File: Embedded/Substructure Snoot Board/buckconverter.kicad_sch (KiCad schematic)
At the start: 33 parts, among them U10 LM5176PWP

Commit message: Added Buck Converter Component Values
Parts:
- removed D3: D_Schottky, symbol Device:D_Schottky
- added C24, C25: 33uF 40mohm, symbol Device:C_Polarized
- added C26: 6.8nF 523mohm, symbol Device:C
- added D3: 500mV 200mA, symbol Device:D
- added Q1, Q2, Q4: CSD17577Q5A, Package_TO_SOT_SMD:TDSON-8-1, symbol Transistor_FET:CSD17577Q5A
- added Q3: CSD17573Q5B, Package_TO_SOT_SMD:TDSON-8-1, symbol Transistor_FET:CSD17573Q5B
- added R18: 4.8m, symbol Device:R
- C10: value C -> 2nF 0ohm
- C11: value C -> 82pF 0ohm
- C12: value C -> 47pF 1mohms
- C13: value C_Polarized -> 33uF 40mohm
- C14, C19: value C -> 47uF 3mohm
- C15: value C -> 100nF 39mohm
- C16, C17, C18: value C -> 22uF 3.71mohm
- C20: value C -> 1uF 11.4mohm
- C21, C22: value C -> 100nF 50mohm
- C23: value C -> 100nF 1mohm
- C8: value C -> 15nF 0ohm
- C9: value C -> 6.8nF 523mohm
- D1, D2: value D_Schottky -> 385mV 500mA
- L1: value L -> 1uH 2.6mohm
- R10, R9: value R -> 100
- R11: value R -> 249K
- R12: value R -> 110K
- R13: value R -> 2K
- R14: value R -> 10
- R15, R16: value R -> 105K
- R17: value R -> 10K
- R6: value R -> 732
- R7: value R -> 93.1K
- R8: value R -> 13K
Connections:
- net GND: now also C19.2, R10.2, R16.2, C24.2, C25.2, R18.2
- net Power Input: now also C24.1, C25.1, Q1.5 (D)
- net Power Output: now also Q3.5 (D)
- net at C20.1, D2.2 (A), R17.1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: now also D3.2 (A)
- net at C21.1, U10.20 (BOOT2): now also D3.1 (K)
- net at C21.2, U10.18 (SW2): now also L1.2, Q3.1 (S), Q3.2 (S), Q3.3 (S), Q4.5 (D)
- net at R9.2: now also Q2.1 (S), Q2.2 (S), Q2.3 (S), Q4.1 (S), Q4.2 (S), Q4.3 (S), R18.1
- net at C9.2, R6.1: now also C26.2
- net at C22.2, U10.28 (SW1): now also L1.1, Q1.1 (S), Q1.2 (S), Q1.3 (S), Q2.5 (D)
- net at C10.1, C9.1, U10.9 (COMP): now also C26.1
- net at U10.19 (HDRV2): now also Q3.4 (G)
- net at U10.21 (LDRV2): now also Q4.4 (G)
- net at U10.25 (LDRV1): now also Q2.4 (G)
- net at U10.27 (HDRV1): now also Q1.4 (G)
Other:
- moved on the sheet: C10, C11, C12, C13, C14, C15, C16, C17, C18, C19, C20, C21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

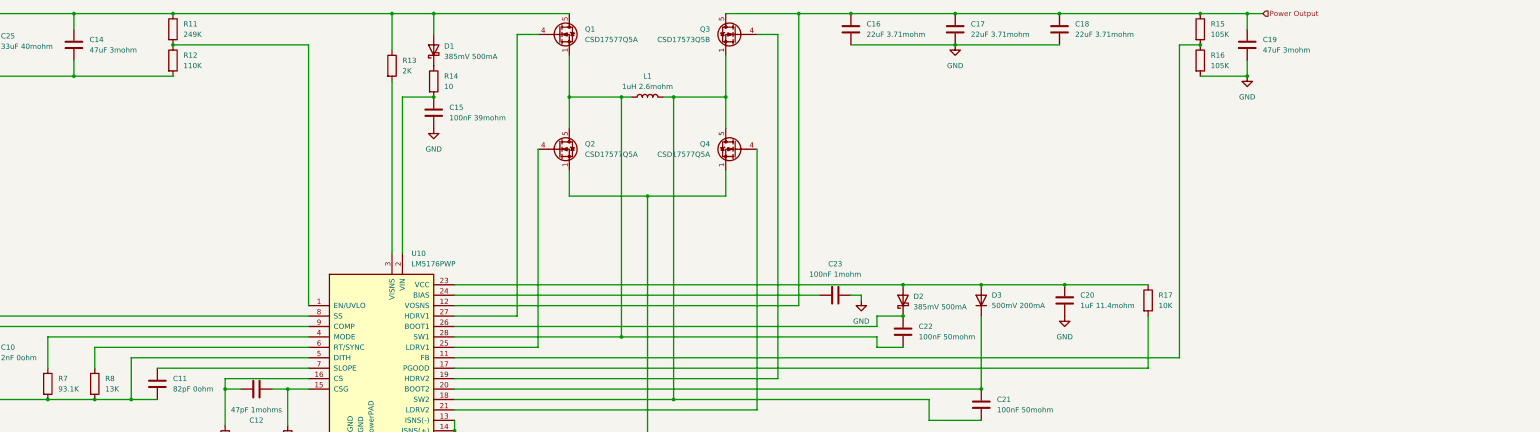
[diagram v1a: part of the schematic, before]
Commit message: Modified Buck Converter (Added Duplicate Components from Reference Design)
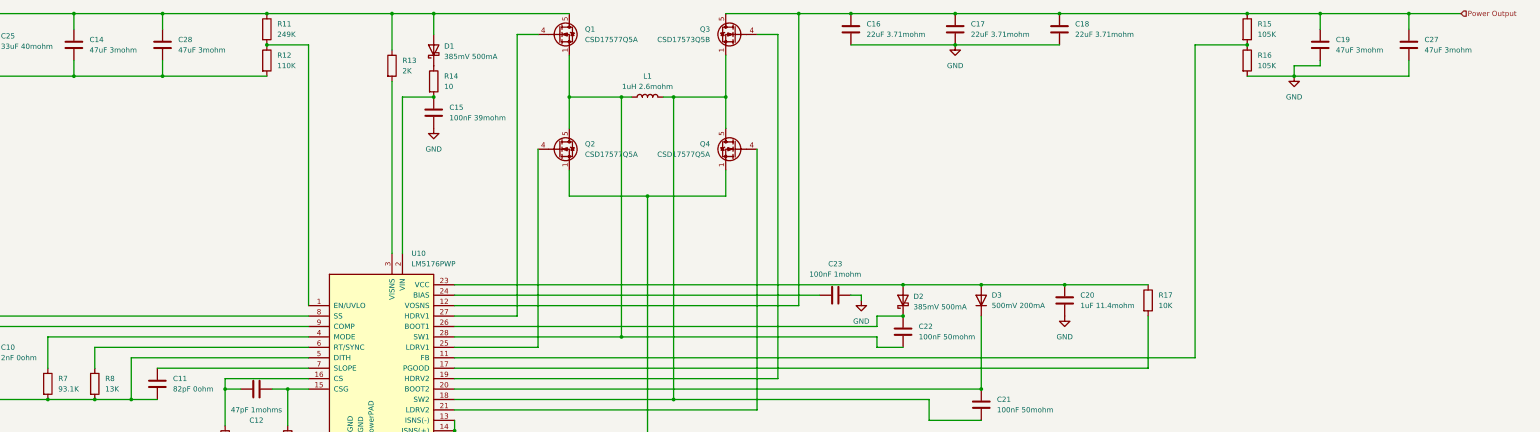
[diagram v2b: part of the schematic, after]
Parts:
- added C27, C28: 47uF 3mohm, symbol Device:C
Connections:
- net GND: now also C27.2, C28.2
- net Power Input: now also C28.1
- net Power Output: now also C27.1
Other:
- moved on the sheet: C19, R11, R12, R15, R16

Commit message: Added Footprints to the Input Power Filtering (Buck Converter)
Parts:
- C13, C24, C25: footprint (none) -> Capacitors:EEFCX1E330R
- C14, C28: footprint (none) -> Capacitor_SMD:C_1210_3225Metric_Pad1.33x2.70mm_HandSolder
- R11, R12: footprint (none) -> Capacitor_SMD:C_0402_1005Metric_Pad0.74x0.62mm_HandSolder
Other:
- moved on the sheet: C10, C11, C12, C13, C14, C15, C16, C17, C18, C19, C20, C21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

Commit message: Added LCSC Parts to Power Input, VCC and Mosfets (Buck Converter)
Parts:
- C13, C24, C25: LCSC (none) -> C193237
- C14, C28: LCSC (none) -> C77101
- C15: footprint (none) -> Resistor_SMD:R_0402_1005Metric_Pad0.72x0.64mm_HandSolder; LCSC (none) -> C2181865
- D1: LCSC (none) -> C155367
- L1: footprint (none) -> Inductors:XAL7070-102ME; LCSC (none) -> C6609502
- Q1, Q2, Q4: LCSC (none) -> C475504
- Q3: LCSC (none) -> C202231
- R11: LCSC (none) -> C482111
- R12: LCSC (none) -> C481928
- R13: footprint (none) -> Capacitor_SMD:C_0402_1005Metric_Pad0.74x0.62mm_HandSolder; LCSC (none) -> C482125
- R14: footprint (none) -> Resistor_SMD:R_0402_1005Metric_Pad0.72x0.64mm_HandSolder; LCSC (none) -> C481926

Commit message: Added Remaining Power Filtering Component LCSC & Footprint (Buck Converter)
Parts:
- C16, C17, C18: footprint (none) -> Capacitor_SMD:C_0603_1608Metric_Pad1.08x0.95mm_HandSolder; LCSC (none) -> C86295
- C19, C27: footprint (none) -> Capacitor_SMD:C_1210_3225Metric_Pad1.33x2.70mm_HandSolder; LCSC (none) -> C77101
- R15: footprint (none) -> Resistor_SMD:R_0603_1608Metric_Pad0.98x0.95mm_HandSolder; LCSC (none) -> C227540
- R16: value 105K -> 20K; footprint (none) -> Resistor_SMD:R_0603_1608Metric_Pad0.98x0.95mm_HandSolder; LCSC (none) -> C105575

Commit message: Added LCSC Components & Footprints to Buck Setup
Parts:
- C10: footprint (none) -> Capacitor_SMD:C_0402_1005Metric_Pad0.74x0.62mm_HandSolder; LCSC (none) -> C1845704
- C11: footprint (none) -> Capacitor_SMD:C_0402_1005Metric_Pad0.74x0.62mm_HandSolder; LCSC (none) -> C650992
- C26, C9: footprint (none) -> Capacitor_SMD:C_0402_1005Metric_Pad0.74x0.62mm_HandSolder; LCSC (none) -> C3840335
- C8: value 15nF 0ohm -> 12nF 0ohm; footprint (none) -> Capacitor_SMD:C_0603_1608Metric_Pad1.08x0.95mm_HandSolder; LCSC (none) -> C519540
- R6: footprint (none) -> Resistor_SMD:R_0402_1005Metric_Pad0.72x0.64mm_HandSolder; LCSC (none) -> C2085222
- R7: footprint (none) -> Resistor_SMD:R_0402_1005Metric_Pad0.72x0.64mm_HandSolder; LCSC (none) -> C2085865
- R8: footprint (none) -> Resistor_SMD:R_0402_1005Metric_Pad0.72x0.64mm_HandSolder; LCSC (none) -> C294438
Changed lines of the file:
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@@
 	)
 	(symbol
+		(lib_id "Device:C")
+		(at 134.62 209.55 0)
+		(unit 1)
+		(exclude_from_sim no)
+		(in_bom yes)
+		(on_board yes)
+		(dnp no)
+		(fields_autoplaced yes)
+		(property "Reference" "C26"
+			(at 138.43 208.2799 0)
+			(effects
+				(font
+					(size 1.27 1.27)
+				)
+				(justify left)
+			)
+		)
+		(property "Value" "6.8nF 523mohm"
+			(at 138.43 210.8199 0)
+			(effects
+				(font
+					(size 1.27 1.27)
+				)
+				(justify left)
+			)
+		)
+		(property "Footprint" "Capacitor_SMD:C_0402_1005Metric_Pad0.74x0.62mm_HandSolder"
+			(at 135.5852 213.36 0)
+			(effects
+				(font
+					(size 1.27 1.27)
+				)
+				(hide yes)
+			)
+		)
+		(property "Datasheet" "~"
+			(at 134.62 209.55 0)
+			(effects
+				(font
+					(size 1.27 1.27)
+				)
+				(hide yes)
+			)
+		)
+		(property "Description" "Unpolarized capacitor"
+			(at 134.62 209.55 0)
+			(effects
+				(font
+					(size 1.27 1.27)
+				)
+				(hide yes)
+			)
+		)
+		(property "LCSC" "C3840335"
+			(at 134.62 209.55 0)
+			(effects
+				(font
+					(size 1.27 1.27)
+				)
+				(hide yes)
+			)
+		)
+		(pin "2"
+		)
+		(pin "1"
+		)
+		(instances
+			(project "Substructure Snoot Board"
+				(path "/f2fe47b0-47e9-4c85-8000-2f6998edcf1c/b8b4d66b-40d9-4643-be7e-3cbb124c7cda"
+					(reference "C26")
+					(unit 1)
+				)
+			)
+		)
+	)
+	(symbol
 		(lib_id "Transistor_FET:CSD17577Q5A")
 		(at 297.18 160.02 0)
@@
 			)
 		)
-		(property "Footprint" ""
+		(property "Footprint" "Resistor_SMD:R_0402_1005Metric_Pad0.72x0.64mm_HandSolder"
 			(at 182.372 217.17 90)
 			(effects
@@
 			)
 		)
+		(property "LCSC" "C294438"
+			(at 184.15 217.17 0)
+			(effects
+				(font
+					(size 1.27 1.27)
+				)
+				(hide yes)
+			)
+		)
 		(pin "1"
 		)
@@
 			)
 		)
-		(property "Value" "15nF 0ohm"
+		(property "Value" "12nF 0ohm"
 			(at 97.79 210.8199 0)
 			(effects
@@
 			)
 		)
-		(property "Footprint" ""
+		(property "Footprint" "Capacitor_SMD:C_0603_1608Metric_Pad1.08x0.95mm_HandSolder"
 			(at 94.9452 213.36 0)
 			(effects
@@
 			)
 		)
+		(property "LCSC" "C519540"
+			(at 93.98 209.55 0)
+			(effects
+				(font
+					(size 1.27 1.27)
+				)
+				(hide yes)
+			)
+		)
 		(pin "2"
 		)
@@
 	)
 	(symbol
-		(lib_id "Device:C")
-		(at 134.62 209.55 0)
-		(unit 1)
-		(exclude_from_sim no)
-		(in_bom yes)
-		(on_board yes)
-		(dnp no)
-		(fields_autoplaced yes)
-		(property "Reference" "C26"
-			(at 138.43 208.2799 0)
-			(effects
-				(font
-					(size 1.27 1.27)
-				)
-				(justify left)
-			)
-		)
-		(property "Value" "6.8nF 523mohm"
-			(at 138.43 210.8199 0)
-			(effects
-				(font
-					(size 1.27 1.27)
-				)
-				(justify left)
-			)
-		)
-		(property "Footprint" ""
-			(at 135.5852 213.36 0)
-			(effects
-				(font
-					(size 1.27 1.27)
-				)
-				(hide yes)
-			)
-		)
-		(property "Datasheet" "~"
-			(at 134.62 209.55 0)
-			(effects
-				(font
-					(size 1.27 1.27)
-				)
-				(hide yes)
-			)
-		)
-		(property "Description" "Unpolarized capacitor"
-			(at 134.62 209.55 0)
-			(effects
-				(font
-					(size 1.27 1.27)
-				)
-				(hide yes)
-			)
-		)
-		(pin "2"
-		)
-		(pin "1"
-		)
-		(instances
-			(project "Substructure Snoot Board"
-				(path "/f2fe47b0-47e9-4c85-8000-2f6998edcf1c/b8b4d66b-40d9-4643-be7e-3cbb124c7cda"
-					(reference "C26")
-					(unit 1)
-				)
-			)
-		)
-	)
-	(symbol
 		(lib_id "Device:R")
 		(at 464.82 130.81 0)
@@
 			)
 		)
-		(property "Footprint" ""
+		(property "Footprint" "Resistor_SMD:R_0402_1005Metric_Pad0.72x0.64mm_HandSolder"
 			(at 121.412 217.17 90)
 			(effects
@@
 			)
 		)
+		(property "LCSC" "C2085222"
+			(at 123.19 217.17 0)
+			(effects
+				(font
+					(size 1.27 1.27)
+				)
+				(hide yes)
+			)
+		)
 		(pin "1"
 		)
@@
 			)
 		)
-		(property "Footprint" ""
+		(property "Footprint" "Resistor_SMD:R_0402_1005Metric_Pad0.72x0.64mm_HandSolder"
 			(at 170.942 217.17 90)
 			(effects
@@
 			)
 		)
+		(property "LCSC" "C2085865"
+			(at 172.72 217.17 0)
+			(effects
+				(font
+					(size 1.27 1.27)
+				)
+				(hide yes)
+			)
+		)
 		(pin "1"
 		)
@@
 			)
 		)
-		(property "Footprint" ""
+		(property "Footprint" "Capacitor_SMD:C_0402_1005Metric_Pad0.74x0.62mm_HandSolder"
 			(at 200.3552 220.98 0)
 			(effects
@@
 			)
 		)
+		(property "LCSC" "C650992"
+			(at 199.39 217.17 0)
+			(effects
+				(font
+					(size 1.27 1.27)
+				)
+				(hide yes)
+			)
+		)
 		(pin "2"
 		)
@@
 			)
 		)
-		(property "Footprint" ""
+		(property "Footprint" "Capacitor_SMD:C_0402_1005Metric_Pad0.74x0.62mm_HandSolder"
 			(at 112.7252 213.36 0)
 			(effects
@@
 			)
 		)
+		(property "LCSC" "C3840335"
+			(at 111.76 209.55 0)
+			(effects
+				(font
+					(size 1.27 1.27)
+				)
+				(hide yes)
+			)
+		)
 		(pin "2"
 		)
@@
 			)
 		)
-		(property "Footprint" ""
+		(property "Footprint" "Capacitor_SMD:C_0402_1005Metric_Pad0.74x0.62mm_HandSolder"
 			(at 158.4452 213.36 0)
 			(effects
@@
 			(at 157.48 209.55 0)
 			(effects
+				(font
+					(size 1.27 1.27)
+				)
+				(hide yes)
+			)
+		)
+		(property "LCSC" "C1845704"
+			(at 157.48 209.55 0)
+			(effects

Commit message: Added LCSC Components & Footprints to Buck Current Sense
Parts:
- C12: footprint (none) -> Capacitor_SMD:C_0402_1005Metric_Pad0.74x0.62mm_HandSolder; LCSC (none) -> C76970
- R10, R9: footprint (none) -> Resistor_SMD:R_0402_1005Metric_Pad0.72x0.64mm_HandSolder; LCSC (none) -> C844713
- R18: value 4.8m -> 5m; footprint (none) -> Resistor_SMD:R_2512_6332Metric_Pad1.40x3.35mm_HandSolder; LCSC (none) -> C22468851
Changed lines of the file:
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@@
+	)
+	(symbol
+		(lib_id "Device:R")
+		(at 231.14 231.14 0)
+		(unit 1)
+		(exclude_from_sim no)
+		(in_bom yes)
+		(on_board yes)
+		(dnp no)
+		(fields_autoplaced yes)
+		(property "Reference" "R10"
+			(at 233.68 229.8699 0)
+			(effects
+				(font
+					(size 1.27 1.27)
+				)
+				(justify left)
+			)
+		)
+		(property "Value" "100"
+			(at 233.68 232.4099 0)
+			(effects
+				(font
+					(size 1.27 1.27)
+				)
+				(justify left)
+			)
+		)
+		(property "Footprint" "Resistor_SMD:R_0402_1005Metric_Pad0.72x0.64mm_HandSolder"
+			(at 229.362 231.14 90)
+			(effects
+				(font
+					(size 1.27 1.27)
+				)
+				(hide yes)
+			)
+		)
+		(property "Datasheet" "~"
+			(at 231.14 231.14 0)
+			(effects
+				(font
+					(size 1.27 1.27)
+				)
+				(hide yes)
+			)
+		)
+		(property "Description" "Resistor"
+			(at 231.14 231.14 0)
+			(effects
+				(font
+					(size 1.27 1.27)
+				)
+				(hide yes)
+			)
+		)
+		(property "LCSC" "C844713"
+			(at 231.14 231.14 0)
+			(effects
+				(font
+					(size 1.27 1.27)
+				)
+				(hide yes)
+			)
+		)
+		(pin "1"
+		)
+		(pin "2"
+		)
+		(instances
+			(project "Substructure Snoot Board"
+				(path "/f2fe47b0-47e9-4c85-8000-2f6998edcf1c/b8b4d66b-40d9-4643-be7e-3cbb124c7cda"
+					(reference "R10")
+					(unit 1)
+				)
+			)
+		)
 	)
 	(symbol
@@
 				(path "/f2fe47b0-47e9-4c85-8000-2f6998edcf1c/b8b4d66b-40d9-4643-be7e-3cbb124c7cda"
 					(reference "R15")
-					(unit 1)
-				)
-			)
-		)
-	)
-	(symbol
-		(lib_id "Device:R")
-		(at 231.14 231.14 0)
-		(unit 1)
-		(exclude_from_sim no)
-		(in_bom yes)
-		(on_board yes)
-		(dnp no)
-		(fields_autoplaced yes)
-		(property "Reference" "R10"
-			(at 233.68 229.8699 0)
-			(effects
-				(font
-					(size 1.27 1.27)
-				)
-				(justify left)
-			)
-		)
-		(property "Value" "100"
-			(at 233.68 232.4099 0)
-			(effects
-				(font
-					(size 1.27 1.27)
-				)
-				(justify left)
-			)
-		)
-		(property "Footprint" ""
-			(at 229.362 231.14 90)
-			(effects
-				(font
-					(size 1.27 1.27)
-				)
-				(hide yes)
-			)
-		)
-		(property "Datasheet" "~"
-			(at 231.14 231.14 0)
-			(effects
-				(font
-					(size 1.27 1.27)
-				)
-				(hide yes)
-			)
-		)
-		(property "Description" "Resistor"
-			(at 231.14 231.14 0)
-			(effects
-				(font
-					(size 1.27 1.27)
-				)
-				(hide yes)
-			)
-		)
-		(pin "1"
-		)
-		(pin "2"
-		)
-		(instances
-			(project "Substructure Snoot Board"
-				(path "/f2fe47b0-47e9-4c85-8000-2f6998edcf1c/b8b4d66b-40d9-4643-be7e-3cbb124c7cda"
-					(reference "R10")
 					(unit 1)
 				)
@@
 			)
 		)
-		(property "Footprint" ""
+		(property "Footprint" "Resistor_SMD:R_0402_1005Metric_Pad0.72x0.64mm_HandSolder"
 			(at 214.122 231.14 90)
 			(effects
@@
 			)
 		)
+		(property "LCSC" "C844713"
+			(at 215.9 231.14 0)
+			(effects
+				(font
+					(size 1.27 1.27)
+				)
+				(hide yes)
+			)
+		)
 		(pin "1"
 		)
@@
 			)
 		)
-		(property "Value" "4.8m"
+		(property "Value" "5m"
 			(at 223.52 237.49 90)
 			(effects
@@
 			)
 		)
-		(property "Footprint" ""
+		(property "Footprint" "Resistor_SMD:R_2512_6332Metric_Pad1.40x3.35mm_HandSolder"
 			(at 223.52 243.078 90)
 			(effects
@@
 		(property "Description" "Resistor"
 			(at 223.52 241.3 0)
+			(effects
+				(font
+					(size 1.27 1.27)
+				)
+				(hide yes)
+			)
+		)
+		(property "LCSC" "C22468851"
+			(at 223.52 241.3 90)
 			(effects
 				(font
@@
 			)
 		)
-		(property "Footprint" ""
+		(property "Footprint" "Capacitor_SMD:C_0402_1005Metric_Pad0.74x0.62mm_HandSolder"
 			(at 227.33 219.4052 0)
 			(effects
@@
 			(effects
 				(font
+					(size 1.27 1.27)
+				)
+				(hide yes)
+			)
+		)
+		(property "LCSC" "C76970"
+			(at 223.52 218.44 90)
+			(effects
+				(font

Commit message: Added LCSC Components & Footprints to Buck Boot Setup
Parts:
- removed D3: 500mV 200mA, symbol Device:D
- added D3: 385mV 500mA, Diode_SMD:D_SOD-123, symbol Device:D_Schottky
- C20: footprint (none) -> Capacitor_SMD:C_0402_1005Metric_Pad0.74x0.62mm_HandSolder; LCSC (none) -> C181015
- C21, C22: footprint (none) -> Capacitor_SMD:C_0603_1608Metric_Pad1.08x0.95mm_HandSolder; LCSC (none) -> C92490
- C23: footprint (none) -> Capacitor_SMD:C_0402_1005Metric_Pad0.74x0.62mm_HandSolder; LCSC (none) -> C133086
- D1: footprint (none) -> Diode_SMD:D_SOD-123
- D2: footprint (none) -> Diode_SMD:D_SOD-123; LCSC (none) -> C398783
- R17: footprint (none) -> Resistor_SMD:R_0402_1005Metric_Pad0.72x0.64mm_HandSolder; LCSC (none) -> C71617
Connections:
- net at C20.1, D2.2 (A), R17.1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: now also D3.2 (A)
- net at C21.1, U10.20 (BOOT2): now also D3.1 (K)
